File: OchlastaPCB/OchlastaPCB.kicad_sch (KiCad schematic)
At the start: 42 parts, among them J1 XT60PW-M, J2 5V, U1 AP64501SP-13, U2 AP3429, U3 STM32F334R8Tx, U4 INA333xxDGK, Y1 Crystal_GND24

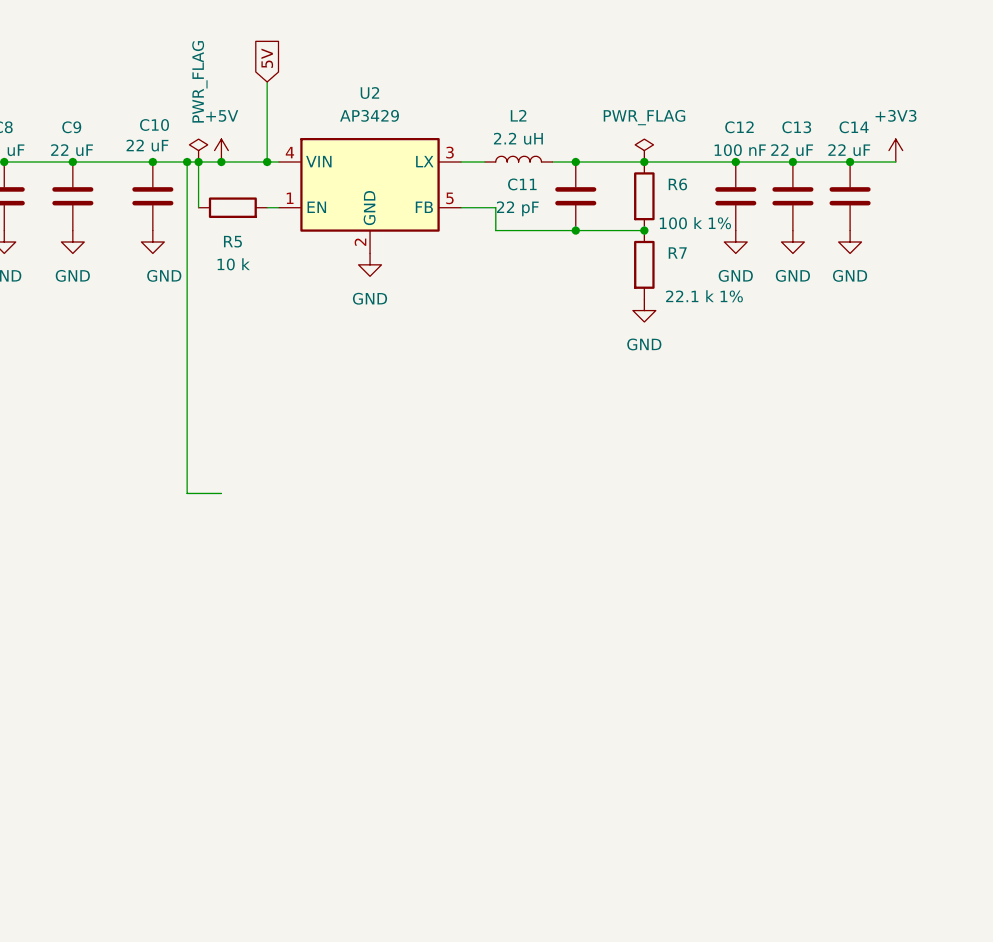
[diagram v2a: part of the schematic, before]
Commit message: Precision LDO for analog circuitry in schematics
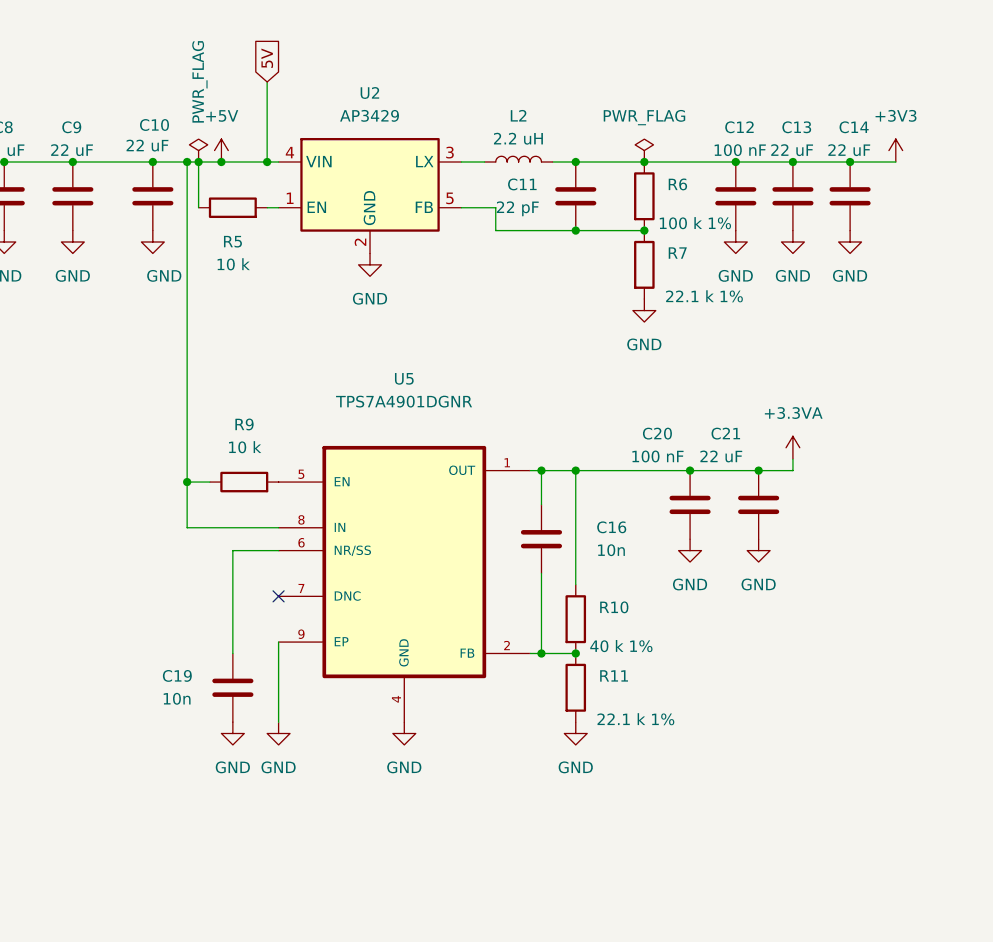
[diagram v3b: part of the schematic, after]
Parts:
- added C16, C19: 10n, symbol Device:C
- added C20: 100 nF, Capacitor_SMD:C_0603_1608Metric, symbol Device:C
- added C21: 22 uF, Capacitor_SMD:C_0805_2012Metric, symbol Device:C
- added R10: 40 k 1%, Resistor_SMD:R_0603_1608Metric, symbol Device:R
- added R11: 22.1 k 1%, Resistor_SMD:R_0603_1608Metric, symbol Device:R
- added R9: 10 k, symbol Device:R
- added U5: TPS7A4901DGNR, TPS7A4901DGNR:SOP65P490X110-9N, symbol TPS7A4901DGNR:TPS7A4901DGNR
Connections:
- net +3.3VA: now also C16.1, C20.1, C21.1, R10.1, U5.1 (OUT)
- net +5V: now also R9.1, U5.8 (IN)
- net GND: now also C19.2, C20.2, C21.2, R11.2, U5.4 (GND), U5.9 (EP)
- new net: C16.2, R10.2, R11.1, U5.2 (FB)
- new net: R9.2, U5.5 (EN)
- new net: C19.1, U5.6 (NR/SS)
- no-connect marks 0 -> 1

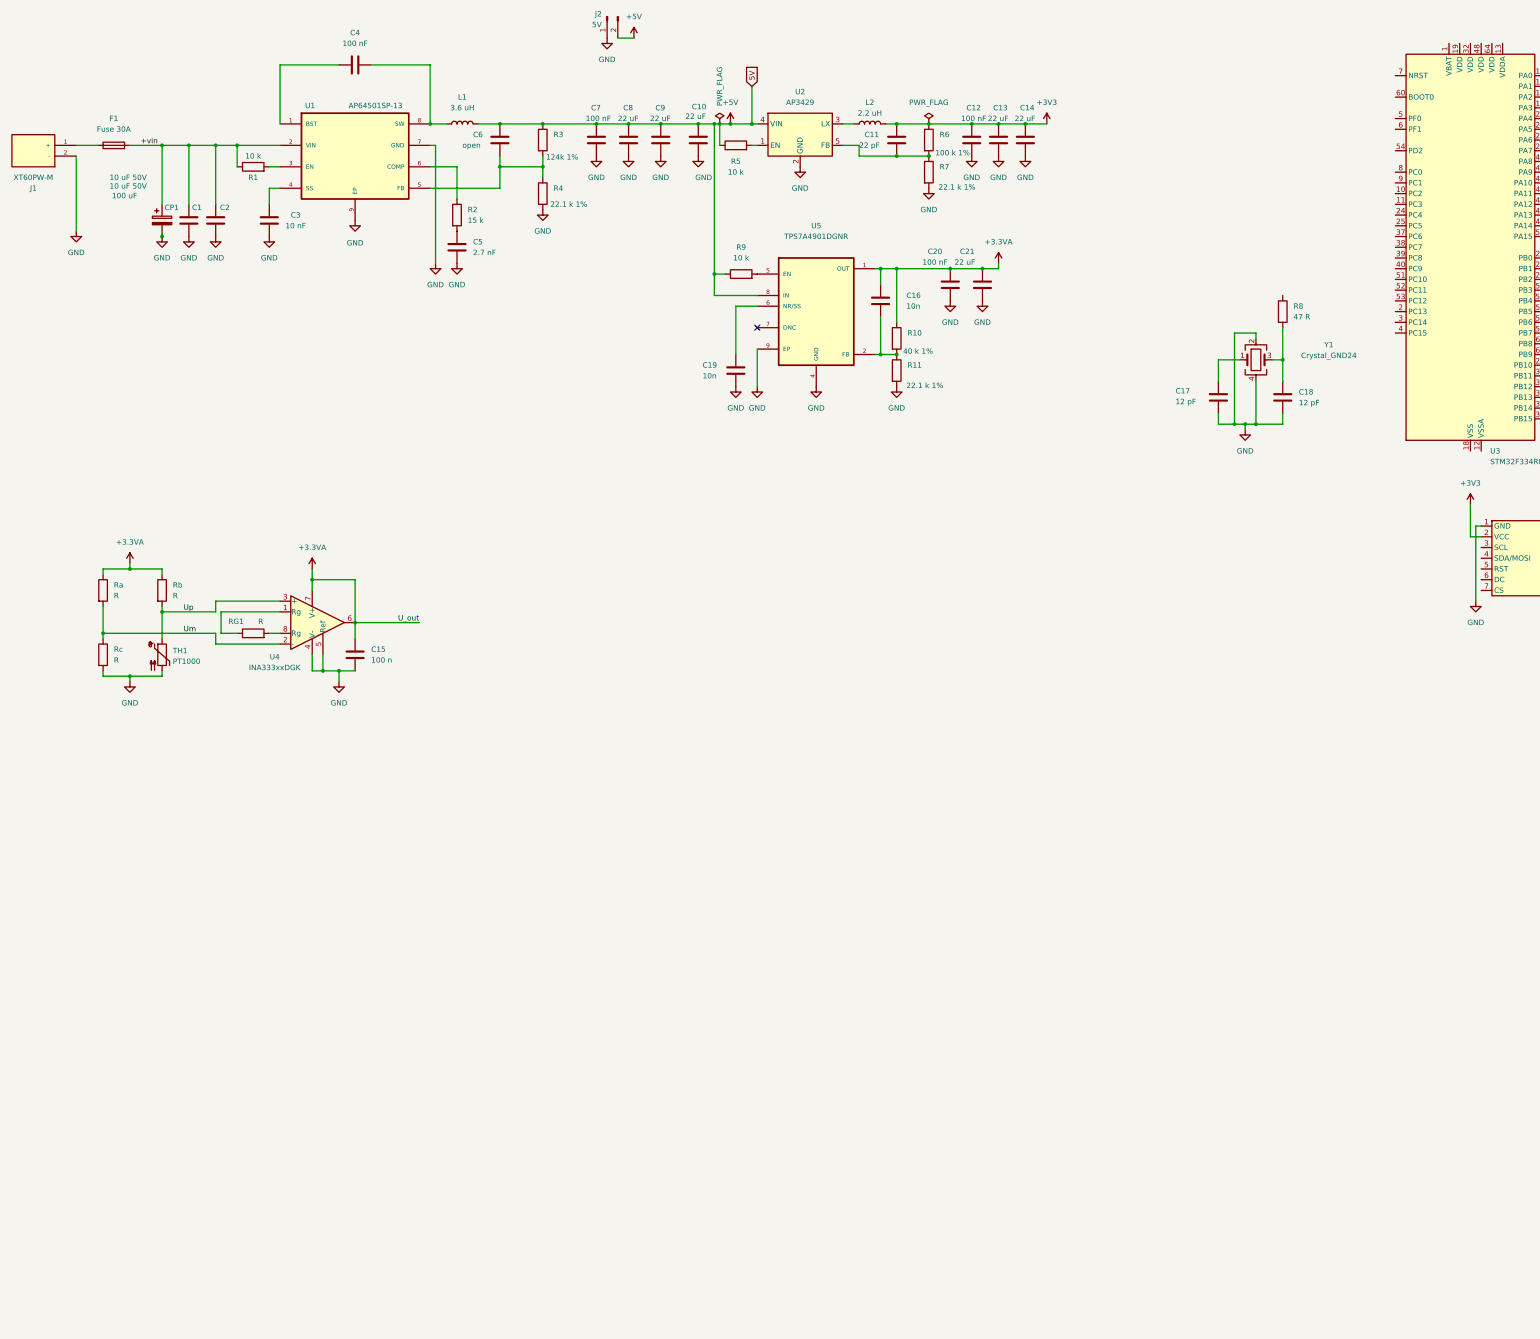
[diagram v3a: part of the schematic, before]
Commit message: Schematics for one channel of main buck converter done I guess
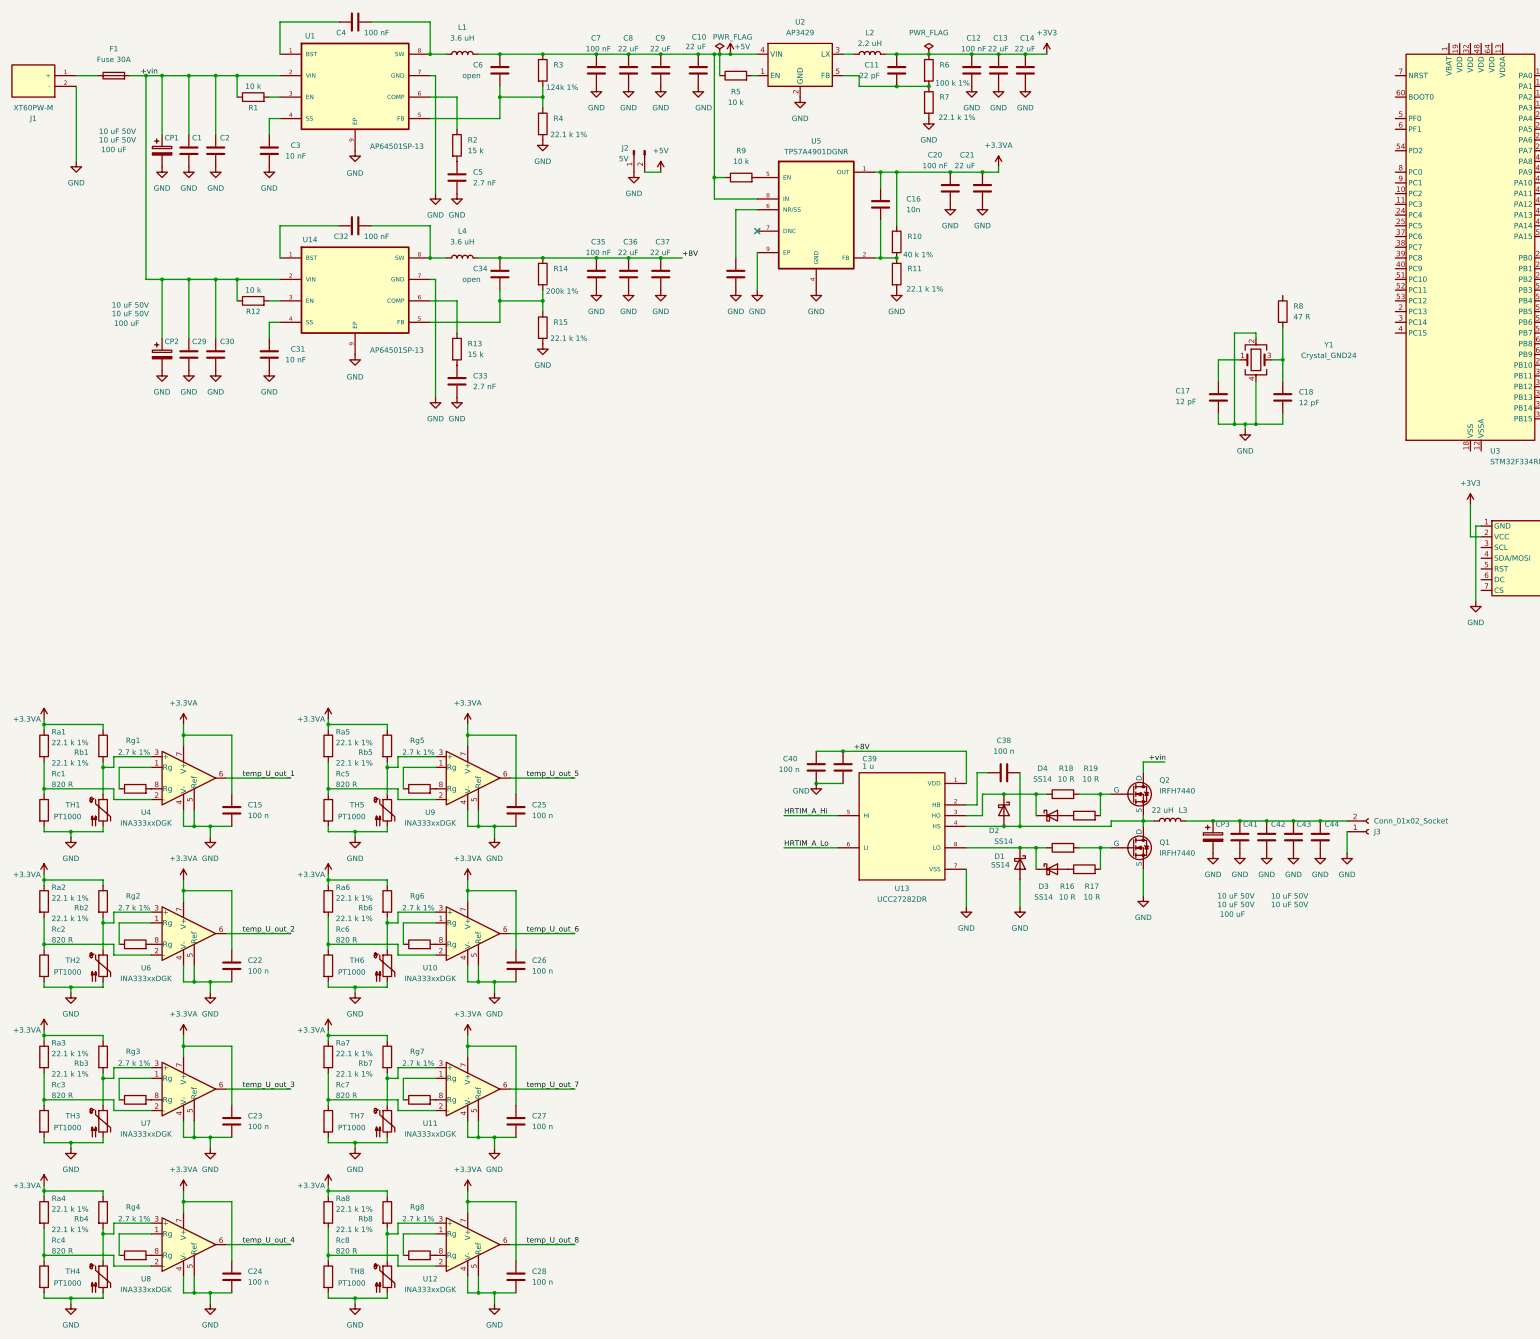
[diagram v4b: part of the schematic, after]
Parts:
- added C22, C23, C24, C25, C26, C27, C28, C38, C40: 100 n, Capacitor_SMD:C_0603_1608Metric, symbol Device:C
- added C29, C30, C41, C42, C43, C44: 10 uF 50V, Capacitor_SMD:C_1206_3216Metric, symbol Device:C
- added C31: 10 nF, Capacitor_SMD:C_0603_1608Metric, symbol Device:C
- added C32, C35: 100 nF, Capacitor_SMD:C_0603_1608Metric, symbol Device:C
- added C33: 2.7 nF, Capacitor_SMD:C_0603_1608Metric, symbol Device:C
- added C34: open, Capacitor_SMD:C_0603_1608Metric, symbol Device:C
- added C36, C37: 22 uF, Capacitor_SMD:C_0805_2012Metric, symbol Device:C
- added C39: 1 u, Capacitor_SMD:C_0603_1608Metric, symbol Device:C
- added CP2, CP3: 100 uF, Capacitor_SMD:CP_Elec_8x10, symbol Device:C_Polarized
- added D1, D2, D3, D4: SS14, Diode_SMD:D_SMA, symbol Device:D_Schottky
- added J3: Conn_01x02_Socket, TerminalBlock_WAGO:TerminalBlock_WAGO_236-402_1x02_P5.00mm_45Degree, symbol Connector:Conn_01x02_Socket
- added L3: 22 uH, Inductor_SMD:L_APV_APH1770, symbol Device:L
- added L4: 3.6 uH, Inductor_SMD:L_Changjiang_FNR4030S, symbol Device:L
- added Q1, Q2: IRFH7440, SnapMagic_downloads:PQFN_5x6_FET, symbol Simulation_SPICE:NMOS
- added R12: 10 k, Resistor_SMD:R_0603_1608Metric, symbol Device:R
- added R13: 15 k, Resistor_SMD:R_0603_1608Metric, symbol Device:R
- added R14: 200k 1%, Resistor_SMD:R_0603_1608Metric, symbol Device:R
- added R15, Ra2, Ra3, Ra4, Ra5, Ra6, Ra7, Ra8, Rb2, Rb3, Rb4, Rb5, Rb6, Rb7, Rb8: 22.1 k 1%, Resistor_SMD:R_0603_1608Metric, symbol Device:R
- added R16, R17, R18, R19: 10 R, Resistor_SMD:R_0603_1608Metric, symbol Device:R
- added Rc2, Rc3, Rc4, Rc5, Rc6, Rc7, Rc8: 820 R, Resistor_SMD:R_0603_1608Metric, symbol Device:R
- added Rg2, Rg3, Rg4, Rg5, Rg6, Rg7, Rg8: 2.7 k 1%, Resistor_SMD:R_0603_1608Metric, symbol Device:R
- added TH2, TH3, TH4, TH5, TH6, TH7, TH8: PT1000, Connector_Phoenix_MC:PhoenixContact_MC_1,5_2-G-3.81_1x02_P3.81mm_Horizontal, symbol Sensor_Temperature:PT1000
- added U10, U11, U12, U6, U7, U8, U9: INA333xxDGK, Package_SO:VSSOP-8_3x3mm_P0.65mm, symbol Amplifier_Instrumentation:INA333xxDGK
- added U13: UCC27282DR, SnapMagic_downloads:SOIC127P599X175-8N, symbol UCC27282DR:UCC27282DR
- added U14: AP64501SP-13, SnapMagic_downloads:SOIC127P600X170-9N, symbol AP64501SP-13:AP64501SP-13
- C15, C16, C19: footprint (none) -> Capacitor_SMD:C_0603_1608Metric
- R9: footprint (none) -> Resistor_SMD:R_0603_1608Metric
- Ra1: renamed from Ra; value R -> 22.1 k 1%; footprint (none) -> Resistor_SMD:R_0603_1608Metric
- Rb1: renamed from Rb; value R -> 22.1 k 1%; footprint (none) -> Resistor_SMD:R_0603_1608Metric
- Rc1: renamed from Rc; value R -> 820 R; footprint (none) -> Resistor_SMD:R_0603_1608Metric
- Rg1: renamed from RG1; value R -> 2.7 k 1%; footprint (none) -> Resistor_SMD:R_0603_1608Metric
- TH1: footprint (none) -> Connector_Phoenix_MC:PhoenixContact_MC_1,5_2-G-3.81_1x02_P3.81mm_Horizontal
- U5: footprint TPS7A4901DGNR:SOP65P490X110-9N -> SnapMagic_downloads:SOP65P490X110-9N
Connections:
- net +3.3VA: now also C22.1, C23.1, C24.1, C25.1, C26.1, C27.1, C28.1, Ra2.1, Ra3.1, Ra4.1, Ra5.1, Ra6.1, Ra7.1, Ra8.1, Rb2.1, Rb3.1, Rb4.1, Rb5.1, Rb6.1, Rb7.1, Rb8.1, U10.7 (V+), U11.7 (V+), U12.7 (V+), U6.7 (V+), U7.7 (V+), U8.7 (V+), U9.7 (V+); no longer U4.6
- net +vin: now also C29.1, C30.1, CP2.1, Q2.1 (D), R12.1, U14.2 (VIN)
- net GND: now also C22.2, C23.2, C24.2, C25.2, C26.2, C27.2, C28.2, C29.2, C30.2, C31.2, C33.2, C35.2, C36.2, C37.2, C39.1, C40.1, C41.2, C42.2, C43.2, C44.2, CP2.2, CP3.2, D1.2 (A), J3.1 (Pin_1), Q1.3 (S), R15.2, Rc2.2, Rc3.2, Rc4.2, Rc5.2, Rc6.2, Rc7.2, Rc8.2, TH2.2, TH3.2, TH4.2, TH5.2, TH6.2, TH7.2, TH8.2, U10.4 (V-), U10.5 (Ref), U11.4 (V-), U11.5 (Ref), U12.4 (V-), U12.5 (Ref), U13.7 (VSS), U14.7 (GND), U14.9 (EP), U6.4 (V-), U6.5 (Ref), U7.4 (V-), U7.5 (Ref), U8.4 (V-), U8.5 (Ref), U9.4 (V-), U9.5 (Ref)
- net Um: no longer names the net of Ra1.2, Rc1.1, U4.2 (-)
- net Up: no longer names the net of Rb1.2, TH1.1, U4.3 (+)
- new net: C41.1, C42.1, C43.1, C44.1, CP3.1, J3.2 (Pin_2), L3.2
- new net: Ra6.2, Rc6.1, U10.2 (-)
- new net: Rb6.2, TH6.1, U10.3 (+)
- new net: D2.1 (K), D4.1 (K), R18.1, U13.3 (HO)
- new net: Q2.2 (G), R18.2, R19.2
- new net: Ra5.2, Rc5.1, U9.2 (-)
- new net: Rg8.1, U12.1 (Rg)
- new net: Rg8.2, U12.8 (Rg)
- new net: C38.1, U13.2 (HB)
- new net: C38.2, D2.2 (A), L3.1, Q1.1 (D), Q2.3 (S), U13.4 (HS)
- new net: D1.1 (K), D3.1 (K), R16.1, U13.8 (LO)
- new net: Rg3.1, U7.1 (Rg)
- new net: Ra3.2, Rc3.1, U7.2 (-)
- new net: Rb3.2, TH3.1, U7.3 (+)
- new net: Rg3.2, U7.8 (Rg)
- new net: Rg7.1, U11.1 (Rg)
- new net: Ra7.2, Rc7.1, U11.2 (-)
- new net: Rb7.2, TH7.1, U11.3 (+)
- new net: Rg7.2, U11.8 (Rg)
- new net: Q1.2 (G), R16.2, R17.2
- new net: Ra8.2, Rc8.1, U12.2 (-)
- new net: D4.2 (A), R19.1
- new net: Rg2.1, U6.1 (Rg)
- new net: Rg2.2, U6.8 (Rg)
- new net: Rb2.2, TH2.1, U6.3 (+)
- new net: C34.2, R14.2, R15.1, U14.5 (FB)
- new net: C32.1, U14.1 (BST)
- new net: R12.2, U14.3 (EN)
- new net: C31.1, U14.4 (SS)
- new net: R13.1, U14.6 (COMP)
- new net: C32.2, L4.1, U14.8 (SW)
- new net: Ra2.2, Rc2.1, U6.2 (-)
- new net: Rb4.2, TH4.1, U8.3 (+)
- new net: C33.1, R13.2
- new net: Rg4.1, U8.1 (Rg)
- new net: Rg4.2, U8.8 (Rg)
- new net: Rb5.2, TH5.1, U9.3 (+)
- new net: Rg6.1, U10.1 (Rg)
- new net: Rg6.2, U10.8 (Rg)
- new net: Ra4.2, Rc4.1, U8.2 (-)
- new net: Rb8.2, TH8.1, U12.3 (+)
- new net: D3.2 (A), R17.1
- new net: Rg5.1, U9.1 (Rg)
- new net: Rg5.2, U9.8 (Rg)
- new net +8V: C34.1, C35.1, C36.1, C37.1, C39.2, C40.2, L4.2, R14.1, U13.1 (VDD)
- new net HRTIM_A_Hi: U13.5 (HI)
- new net HRTIM_A_Lo: U13.6 (LI)
- new net temp_U_out_1: U4.6
- new net temp_U_out_2: U6.6
- new net temp_U_out_3: U7.6
- new net temp_U_out_4: U8.6
- new net temp_U_out_5: U9.6
- new net temp_U_out_6: U10.6
- new net temp_U_out_7: U11.6
- new net temp_U_out_8: U12.6
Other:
- moved on the sheet: C1, C10, C11, C12, C13, C14, C15, C16, C2, C20, C21, C3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
